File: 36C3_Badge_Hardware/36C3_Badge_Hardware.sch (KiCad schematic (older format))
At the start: 155 parts, among them J1 MicroUSB, J2 ISP, Q1 FS8205A, Q10 MMBTA42, Q2 MMBTA42, Q3 MMBTA42, Q4 MMBTA92, Q5 MMBTA42, Q6 MMBTA42, Q7 MMBTA42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

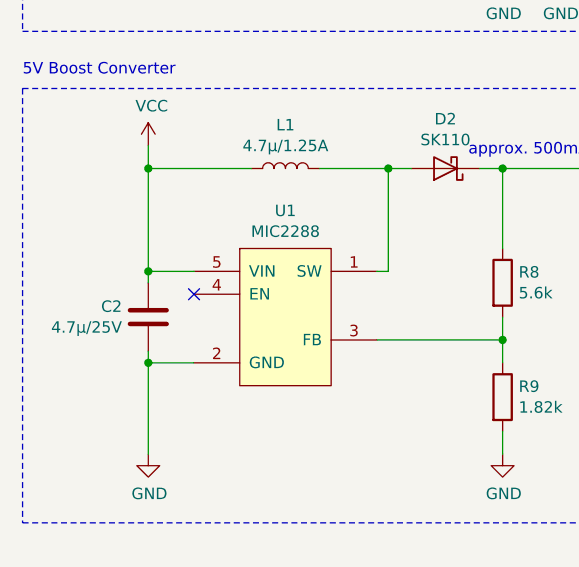
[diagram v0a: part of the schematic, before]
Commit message: Fixed EN of boost converter not being tied to VIN
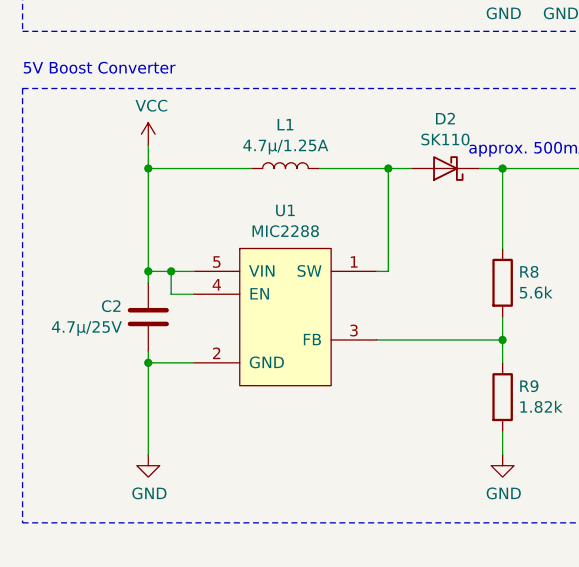
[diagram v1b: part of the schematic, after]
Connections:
- net VCC: now also U1.4 (EN)
- no-connect marks 9 -> 8
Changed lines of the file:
@@
 	1450 9150 1450 9100
 Wire Wire Line
-	1450 9100 1650 9100
+	1450 9100 1550 9100
 Wire Wire Line
 	1450 9450 1450 9500
@@
 	1450 9500 1450 9900
 Connection ~ 1450 9500
-NoConn ~ 1650 9200
 Wire Wire Line
 	1450 9100 1450 8650
@@
 	5800 3650 5800 3850
 $Comp
-L custom:VCC #PWR?
+L custom:VCC #PWR0102
 U 1 1 5E25C45B
 P 1450 8550
-F 0 "#PWR?" H 1450 8400 50  0001 C CNN
+F 0 "#PWR0102" H 1450 8400 50  0001 C CNN
 F 1 "VCC" H 1465 8723 50  0000 C CNN
 F 2 "" H 1450 8550 50  0001 C CNN
@@
 	1    0    0    -1
 $EndComp
+Wire Wire Line
+	1650 9200 1550 9200
+Wire Wire Line
+	1550 9200 1550 9100
+Connection ~ 1550 9100
+Wire Wire Line
+	1550 9100 1650 9100
 $EndSCHEMATC

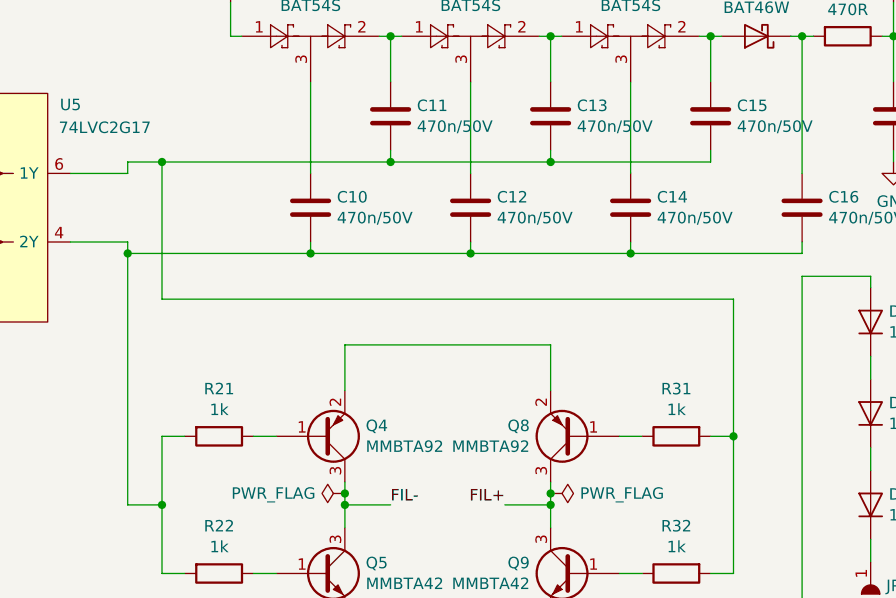
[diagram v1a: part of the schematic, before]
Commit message: Fixed missing +5V connection to VFD filament H-bridge
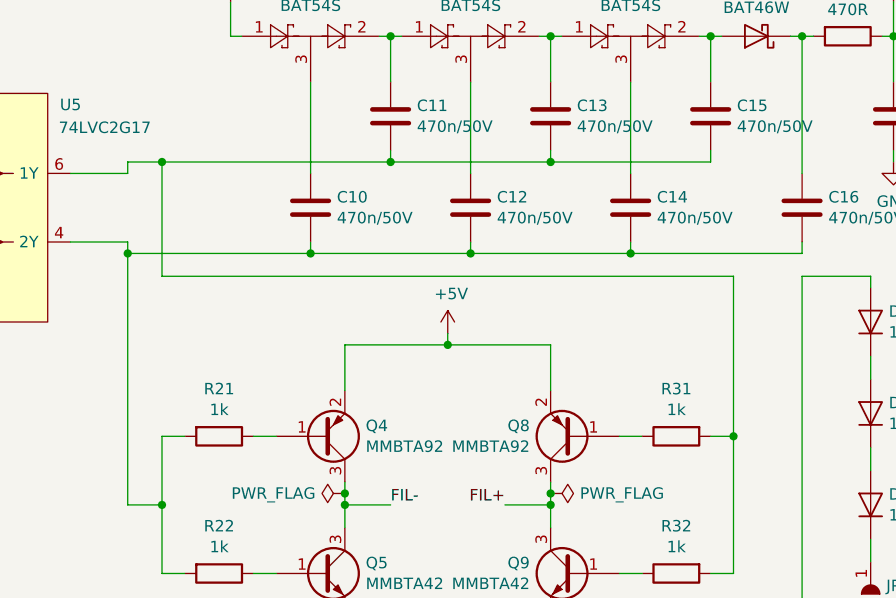
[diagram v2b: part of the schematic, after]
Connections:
- net +5V: now also Q4.2 (E), Q8.2 (E)
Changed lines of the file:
@@
 	9150 2800 9150 2600
 Wire Wire Line
-	9150 2600 10050 2600
+	9150 2600 9600 2600
 Wire Wire Line
 	10050 2600 10050 2800
@@
 	8350 3300 8350 3600
 Wire Wire Line
-	10850 2400 8350 2400
+	10850 2300 8350 2300
 Wire Wire Line
-	8350 2400 8350 1800
+	8350 2300 8350 1800
 Connection ~ 10850 3000
 Wire Wire Line
@@
 	8200 2200 9000 2200
 Wire Wire Line
-	10850 2400 10850 3000
+	10850 2300 10850 3000
 $Comp
 L power:GND #PWR040
@@
 Wire Wire Line
 	1550 9100 1650 9100
+Wire Wire Line
+	9600 2550 9600 2600
+Connection ~ 9600 2600
+Wire Wire Line
+	9600 2600 10050 2600
+$Comp
+L power:+5V #PWR?
+U 1 1 5E3B59F3
+P 9600 2550
+F 0 "#PWR?" H 9600 2400 50  0001 C CNN
+F 1 "+5V" H 9615 2723 50  0000 C CNN
+F 2 "" H 9600 2550 50  0001 C CNN
+F 3 "" H 9600 2550 50  0001 C CNN
+	1    9600 2550
+	1    0    0    -1
+$EndComp
 $EndSCHEMATC
